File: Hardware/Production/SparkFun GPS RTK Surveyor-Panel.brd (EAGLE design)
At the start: 166 x 248 mm, 778 parts, among them J13 Internal, J16 microSD, J17 Qwiic Right Angle, J19 External, J20 USB Female Type C Connector, J21 Power Switch, J24 Start Base, J25 USB Female Type C Connector, J3 USB Female Type C Connector, J32 microSD, J34 Qwiic Right Angle, J36 Internal, J37 External, J38 USB Female Type C Connector, J39 Power Switch, J4 External, J42 Start Base, J43 USB Female Type C Connector, J5 USB Female Type C Connector, J50 microSD, J52 Qwiic Right Angle, J54 Internal, J55 External, J56 USB Female Type C Connector, J57 Power Switch, J6 Start Base, J60 Start Base, J61 USB Female Type C Connector, J68 microSD, J7 Power Switch, J70 Qwiic Right Angle, J72 Internal, Q1 MBT3904DW1T1, Q2 MBT3904DW1T1, Q3 MBT3904DW1T1, Q4 MBT3904DW1T1, U1 3.3V, U10 MCP73833, U11 CH340C, U12 MAX17048, U13 3.3V, U14 MCP73833, U15 3.3V, U16 U-BLOX_ZED-F9P, U17 ESP-WROOM-32NARROW, U18 CH340C, U19 MAX17048, U2 3.3V, U20 3.3V, U21 MCP73833, U22 3.3V, U23 U-BLOX_ZED-F9P, U24 ESP-WROOM-32NARROW, U25 CH340C, U26 MAX17048, U27 3.3V, U28 MCP73833, U3 U-BLOX_ZED-F9P, U4 3.3V, U5 ESP-WROOM-32NARROW, U6 CH340C, U7 MAX17048, U8 U-BLOX_ZED-F9P, U9 ESP-WROOM-32NARROW

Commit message: 1x3 panel
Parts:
- removed BLUETOOTH_BROADCAST3, SERIAL1_CONNECTION3, ZED_CONTROL3: (no value), SparkFun-Switches:SWITCH_DPDT_SMD_AYZ0202
- removed BT4: LIPO-OUTLINE1100, SparkFun-Batteries:LIPO-1000
- removed C52, C54, C56, C67, C68: 1.0uF, SparkFun-Capacitors:0603
- removed C53, C57, C61, C62, C63, C65, C66: 0.1uF, SparkFun-Capacitors:0603
- removed C55: 47pF, SparkFun-Capacitors:0402
- removed C58, C59: 4.7uF, SparkFun-Capacitors:0603
- removed C60, C64: 10uF, SparkFun-Capacitors:0603
- removed D37: Yellow, SparkFun-LED:LED-0603
- removed D38: WHITE, SparkFun-LED:LED-0603
- removed D39, D48: PRTR5V0U2F, SparkFun-IC-Power:SOT886
- removed D40: RED, SparkFun-LED:LED-0603
- removed D41, D46: 3A/10V/280mV, SparkFun-DiscreteSemi:SOD-323
- removed D42, D43, D44: GREEN, SparkFun-LED:LED-0603
- removed D45: BLUE, SparkFun-LED:LED-0603
- removed D47: RGB, SparkFun-LED:PLCC-6-LED
- removed DUAL_OUTPUT3: (no value), SparkFun-Jumpers:SMT-JUMPER_2_NO_SILK
- removed E4: SMA, SparkFun-RF:SMA-EDGE-SMD
- removed FB4: 2.66Ω, SparkFun-Coils:0402-TIGHT
- removed J55: External, SparkFun-Connectors:JST04_1MM_RA
- removed J56, J61: USB Female Type C Connector, SparkFun-Connectors:USB-C-16P_4LAYER-PADS
- removed J57: Power Switch, SparkFun-Connectors:JST-2-SMD
- removed J58: (no value), SparkFun-Connectors:JST-2-SMD
- removed J59, J67, J69: (no value), SparkFun-Connectors:1X02_NO_SILK
- removed J60: Start Base, SparkFun-Connectors:JST-2-SMD
- removed J62, J63: (no value), SparkFun-Connectors:JST-4-SMD-1.25MM-LOCKING
- removed J64, J65, J66: (no value), SparkFun-Connectors:1X04_NO_SILK
- removed J68: microSD, SparkFun-Connectors:MICRO-SD-SOCKET
- removed J70: Qwiic Right Angle, SparkFun-Connectors:1X04_NO_SILK
- removed J71: (no value), SparkFun-Connectors:1X05_NO_SILK
- removed J72: Internal, SparkFun-Connectors:JST04_1MM_RA
- removed JP10, JP11, JP12, JP9: FIDUCIALUFIDUCIAL, SparkFun-Aesthetics:FIDUCIAL-MICRO
- removed LOGO10: OSHW-LOGOMINI, SparkFun-Aesthetics:OSHW-LOGO-MINI
- removed LOGO11, LOGO12: SFE_LOGO_NAME_FLAME.1_INCH, SparkFun-Aesthetics:SFE_LOGO_NAME_FLAME_.1
- removed MEAS6, MEAS7: (no value), SparkFun-Jumpers:COMBO-JUMPER_2_NC_TRACE
- removed Q4: MBT3904DW1T1, SparkFun-DiscreteSemi:SC70-6
- removed R100, R113, R99: 33, SparkFun-Resistors:1206_RA
- removed R101: 33, SparkFun-Resistors:0603
- removed R102, R112, R94: 330, SparkFun-Resistors:0603
- removed R103, R116, R117: 1k, SparkFun-Resistors:0603
- removed R104, R105, R106, R91: 20, SparkFun-Resistors:0603
- removed R107, R108, R109, R120: 10k, SparkFun-Resistors:0603
- removed R110, R111, R97, R98: 5.1k, SparkFun-Resistors:0603
- removed R114, R96: 100k, SparkFun-Resistors:0603
- removed R115: 4.7k, SparkFun-Resistors:0603
- removed R118: 150k, SparkFun-Resistors:0603
- removed R119: 0, SparkFun-Resistors:0603
- removed R92, R93: 27, SparkFun-Resistors:0603
- removed R95: 10, SparkFun-Resistors:0603
- removed U$277, U$368: (no value), SparkFun-Aesthetics:QWIIC_4MM
- removed U$278: (no value), output:#RTK#0
- removed U$279: (no value), output:#PPS#1
- removed U$280: (no value), output:#PWR#2
- removed U$281, U$309, U$350: (no value), output:#3V3#0
- removed U$282, U$310, U$311, U$353: (no value), output:#GND#0
- removed U$283: (no value), output:ANTENNA0
- removed U$284, U$335: (no value), output:_SURVEYOR3
- removed U$285: (no value), output:#RTK#1
- removed U$286: (no value), output:ACTIVE0
- removed U$287: (no value), output:L1#L21
- removed U$288: (no value), output:#PAIR#0
- removed U$289: (no value), SparkFun GPS RTK Surveyor:1553DBK-ENCLOSURE
- removed U$290: (no value), output:#CHG#0
- removed U$291: (no value), output:LIPO0
- removed U$292: (no value), output:U#BLOX0
- removed U$293, U$348: (no value), output:USB1
- removed U$294: (no value), output:SERIAL20
- removed U$295, U$331: (no value), output:SERIAL10
- removed U$296, U$298: (no value), SparkFun GPS RTK Surveyor:ROCKER_SWITCH
- removed U$297: (no value), output:#BASE#0
- removed U$299, U$300, U$333, U$340, U$341, U$342, U$343, U$344: (no value), SparkFun GPS RTK Surveyor:LIGHT_PIPE_3MM
- removed U$301: (no value), output:BASE2
- removed U$302: (no value), output:OFF1
- removed U$303: (no value), output:ON0
- removed U$304: (no value), output:ROVER3
- removed U$305: (no value), output:#RX2#2
- removed U$306: (no value), output:#TX2#1
- removed U$307, U$352: (no value), output:#RX1#2
- removed U$308, U$351: (no value), output:#TX1#1
- removed U$312, U$325: (no value), output:NMEA1
- removed U$313: (no value), output:RADIO0
- removed U$314: (no value), output:##RST##4
- removed U$315: (no value), output:##SAFE##5
- removed U$316: (no value), output:#FENCE#3
- removed U$317: (no value), output:#INT#0
- removed U$318: (no value), output:BASE0
- removed U$319, U$321: (no value), output:SWITCH1
- removed U$320: (no value), output:POWER0
- removed U$322: (no value), output:#3#5#5V#0
- removed U$323: (no value), output:BLUETOOTH2
- removed U$324: (no value), output:BROADCAST3
- removed U$326: (no value), output:RTCM0
- removed U$327: (no value), output:BLUEOOTH3
- removed U$328: (no value), output:CNTR1
- removed U$329: (no value), output:EXT0
- removed U$330: (no value), output:NMEA2
- removed U$332: (no value), output:CONNECTION1
- removed U$334: (no value), output:#PPS#0
- removed U$336: (no value), output:#RX#2
- removed U$337: (no value), output:ZED0
- removed U$338: (no value), output:#TX#1
- removed U$339: (no value), output:#DUAL#0
- removed U$345: (no value), output:#1CM#0
- removed U$346: (no value), output:#10CM#1
- removed U$347: (no value), output:#100CM#2
- removed U$349: (no value), output:ESP320
- removed U$354: (no value), output:MICROSD0
- removed U$355: (no value), output:#GND#1
- removed U$356: (no value), output:#ESP_RST#0
- removed U$357, U$358: (no value), output:RTK0
- removed U$359: (no value), output:#GND#2
- removed U$360: (no value), output:#3V3#2
- removed U$361: (no value), output:#SCL#1
- removed U$362: (no value), output:#SDA#0
- removed U$363: (no value), output:#D_SEL#0
- removed U$364: (no value), output:DATA2
- removed U$365: (no value), output:PORT3
- removed U$366: (no value), output:PPS#RESET0
- removed U$367: (no value), output:NMEA#SERIAL1
- removed U22, U27: 3.3V, SparkFun-IC-Power:SOT23-5
- removed U23: U-BLOX_ZED-F9P, SparkFun-GPS:ZED-F9P
- removed U24: ESP-WROOM-32NARROW, SparkFun-RF:ESP-WROOM-32-NARROW
- removed U25: CH340C, SparkFun-IC-Comms:SO016
- removed U26: MAX17048, SparkFun-IC-Power:DFN-8
- removed U28: MCP73833, SparkFun-IC-Power:DFN-10
- moved BLUETOOTH_BROADCAST2 180.4 mm to (150.0, 19.0)
- moved BT3 180.4 mm to (197.0, 63.4)
- moved C35 180.4 mm to (174.1, 38.0)
- moved C36 180.4 mm to (171.6, 38.0)
- moved C37 180.4 mm to (180.5, 40.6)
- moved C38 180.4 mm to (167.8, 16.2)
- moved C39 180.4 mm to (176.7, 38.0)
- moved C40 180.4 mm to (172.8, 40.6)
- moved C41 180.4 mm to (153.8, 105.3)
- moved C42 180.4 mm to (153.8, 98.0)
- moved C43 180.4 mm to (156.3, 94.9)
- moved C44 180.4 mm to (181.7, 99.0)
- moved C45 180.4 mm to (184.3, 95.2)
- moved C46 180.4 mm to (183.3, 99.0)
- moved C47 180.4 mm to (156.3, 96.5)
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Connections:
- removed net 3.3V3: C52.1, C53.2, C56.1, C57.2, C60.1, C61.1, C63.1, C64.1, C65.1, J55.2, J63.1, J65.4, J66.4, J68.VCC, J70.2, J72.2, R107.2, R114.2, R94.2, R96.2, U22.5, U23.33, U23.34, U23.38, U24.2, U25.16, U25.4
- removed net 5V3: C54.1, J57.1, J62.1, J64.4, U22.1, U22.3
- removed net ANT_VCC3: C55.1, FB4.2, R95.1
- removed net BACKUP3: C68.1, U23.36, U27.5
- removed net CC13: J56.A5, R98.2
- removed net CC14: J56.B5, R97.2
- removed net CC15: J61.B5, R110.2
- removed net CC16: J61.A5, R111.2
- removed net CHG_LED3: R115.2, U28.3
- removed net CHG_THERM4: R118.2, R119.2, R120.2
- removed net D+6: D39.4, R92.1
- removed net D+7: D48.4, U25.5
- removed net D-6: D39.6, R93.1
- removed net D-7: D48.6, U25.6
- removed net ESP32_!DTR3: Q4.1, R108.1, U25.13
- removed net ESP32_!RTS3: Q4.4, R109.1, U25.14
- removed net ESP32_EN3: C62.1, J69.1, Q4.3, R107.1, U24.3
- removed net ESP32_RXI3: U24.34, U25.2
- removed net ESP32_TXO3: U24.35, U25.3
- removed net ESP_0/BOOT3: Q4.6, U24.25
- removed net ESP_12/LED_BLUETOOTH3: R112.1, U24.14
- removed net ESP_13/LED_100CM3: R104.1, U24.16
- removed net ESP_15/LED_10CM3: R105.1, U24.23
- removed net ESP_16/BT_RXI3: BLUETOOTH_BROADCAST3.2, U24.27
- removed net ESP_17/BT_TXO3: BLUETOOTH_BROADCAST3.5, U24.28
- removed net ESP_18/SD_SCK3: J68.SCLK, U24.30
- removed net ESP_19/SD_CIPO3: J68.DO/DAT0, U24.31
- removed net ESP_2/LED_1CM3: R106.1, U24.24
- removed net ESP_21/SDA3: J55.3, J70.3, J72.3, R99.P6, U24.33, U26.8
- removed net ESP_22/SCL3: J55.4, J70.4, J72.4, R99.P7, U24.36, U26.7
- removed net ESP_23/SD_COPI3: J68.DI/CMD, U24.37
- removed net ESP_25/SD_!CS!3: J68.CS/DAT3, R114.1, U24.10
- removed net ESP_26/ZED_TX_READY3: J71.1, R99.P8, U24.11
- removed net ESP_26/ZED_TX_READY_LV3: R99.P1, U23.46
- removed net ESP_27/ZED_!RESET!3: J71.2, R100.P5, U24.12, ZED_CONTROL3.4
- removed net ESP_27/ZED_!RESET!_LV3: R100.P4, U23.49
- removed net ESP_3: U24.13
- removed net ESP_32/PWR_LVL_RED3: D47.AR, U24.8
- removed net ESP_33/PWR_LVL_GRN3: D47.AG, U24.9
- removed net ESP_36/BATT_ALRT3: U24.4, U26.5
- removed net ESP_4/LED_BASE_STAT3: R102.1, U24.26
- removed net ESP_5/SWITCH_BASE_SELECT3: J60.1, U24.29
- removed net ESP_D1+3: D48.3, J61.A6, J61.B6
- removed net ESP_D1-3: D48.1, J61.A7, J61.B7
- removed net ESP_I7: U24.5
- removed net ESP_I8: U24.6
- removed net ESP_I9: U24.7
- removed net EXTERNAL_SERIAL1_RXI/ZED_!RESET!3: J63.3, J65.2, ZED_CONTROL3.5
- removed net EXTERNAL_SERIAL1_RXI3: SERIAL1_CONNECTION3.4, ZED_CONTROL3.6
- removed net EXTERNAL_SERIAL1_TXO/PPS3: J63.2, J65.3, ZED_CONTROL3.2
- removed net EXTERNAL_SERIAL1_TXO3: DUAL_OUTPUT3.2, SERIAL1_CONNECTION3.1, ZED_CONTROL3.3
- removed net FENCE_LV3: R113.P8, U23.19
- removed net GND3: C52.2, C53.1, C54.2, C55.2, C56.2, C57.1, C58.2, C59.2, C60.2, C61.2, C62.2, C63.2, C64.2, C65.2, C66.2, C67.2, C68.2, D37.C, D39.2, D40.C, D42.C, D43.C, D44.C, D45.C, D48.2, E4.GND@0, E4.GND@1, J55.1, J56.GND, J56.GND2, J56.SHLD1, J56.SHLD2, J56.SHLD3, J56.SHLD4, J58.1, J59.2, J60.2, J61.GND, J61.GND2, J61.SHLD1, J61.SHLD2, J61.SHLD3, J61.SHLD4, J62.4, J63.4, J64.1, J65.1, J66.1, J68.CD1, J68.GND, J68.GND1, J68.GND3, J69.2, J70.1, J72.1, R103.1, R110.1, R111.1, R116.2, R117.2, R118.1, R120.1, R96.1, R97.1, R98.1, U22.2, U23.1, U23.100, U23.101, U23.102, U23.12, U23.14, U23.3, U23.32, U23.37, U23.41, U23.48, U23.55, U23.56, U23.57, U23.58, U23.59, U23.60, U23.61, U23.62, U23.63, U23.64, U23.65, U23.66, U23.67, U23.68, U23.69, U23.70, U23.71, U23.72, U23.73, U23.74, U23.75, U23.76, U23.77, U23.78, U23.79, U23.80, U23.81, U23.82, U23.83, U23.84, U23.85, U23.86, U23.87, U23.88, U23.89, U23.90, U23.91, U23.92, U23.93, U23.94, U23.95, U23.96, U23.97, U23.98, U23.99, U24.1, U24.15, U24.38, U24.GND, U25.1, U26.1, U26.4, U26.6, U26.9, U27.2, U28.11, U28.5
- removed net GPS_ANT4: E4.SIG, FB4.1, U23.2
- removed net LIPO_RAW3: J58.2, MEAS7.1, MEAS7.3
- removed net N$55: D37.A, R91.1
- removed net N$56: R92.2, U23.40
- removed net N$57: R93.2, U23.39
- removed net N$58: D38.A, R94.1
- removed net N$59: R95.2, U23.7
- removed net N$60: D40.A, R102.2
- removed net N$61: D42.A, R104.2
- removed net N$62: D43.A, R105.2
- removed net N$63: D44.A, R106.2
- removed net N$64: Q4.5, R108.2
- removed net N$65: Q4.2, R109.2
- removed net N$66: D46.A, J61.VBUS1, J61.VBUS2
- removed net N$67: D45.A, R112.2
- removed net N$68: J56.VBUS1, J56.VBUS2, MEAS6.1, MEAS6.3
- removed net N$69: D47.CG, R116.1
- removed net N$70: D47.CR, R117.1
- removed net N$71: D47.CB, R115.1
- removed net N$72: R119.1, U28.8
- removed net NMEA-RX3: BLUETOOTH_BROADCAST3.6, SERIAL1_CONNECTION3.6
- removed net NMEA-TX3: BLUETOOTH_BROADCAST3.3, DUAL_OUTPUT3.1, SERIAL1_CONNECTION3.3
- removed net PPS3: R100.P1, U23.53
- removed net PROG4: R103.2, U28.6
- removed net RTK_LV3: R113.P7, U23.20
- removed net RX2_LV3: R113.P6, U23.26
- removed net RXLV3: R99.P4, U23.43
- removed net SCL_LV3: R99.P2, U23.45
- removed net SDA_LV3: R99.P3, U23.44
- removed net TX2_LV3: R113.P5, U23.27
- removed net TXLV3: R101.1, U23.42
- removed net UNP_D+3: D39.3, J56.A6, J56.B6
- removed net UNP_D-3: D39.1, J56.A7, J56.B7
- removed net VIN3: C59.1, D39.5, D41.C, D46.C, D47.AB, D48.5, J57.2, MEAS6.2, MEAS6.4, U28.1, U28.2
- removed net V_BATT3: C58.1, C66.1, C67.1, D41.A, J59.1, MEAS7.2, MEAS7.4, U26.2, U26.3, U27.1, U27.3, U28.10, U28.9
- removed net ZED-RXI7: BLUETOOTH_BROADCAST3.4, J62.3, J64.2, R113.P3
- removed net ZED-RXI8: J67.2, R99.P5, SERIAL1_CONNECTION3.5
- removed net ZED-TXO7: J67.1, R101.2, SERIAL1_CONNECTION3.2
- removed net ZED-TXO8: BLUETOOTH_BROADCAST3.1, J62.2, J64.3, R113.P4
- removed net ZED_!SAFE!3: J71.3, R100.P6
- removed net ZED_!SAFE!_LV3: R100.P3, U23.50
- removed net ZED_D_SEL3: J71.5, R100.P7
- removed net ZED_D_SEL_LV3: R100.P2, U23.47
- removed net ZED_FENCE_STAT3: J66.2, R113.P1
- removed net ZED_PPS_STAT3: J71.4, R100.P8, R91.2, ZED_CONTROL3.1
- removed net ZED_RTK_STAT3: D38.C, J66.3, R113.P2
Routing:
- net 3.3V3: track 297.3 -> 0.00 mm, vias 8 -> 0
- net ESP_22/SCL3: track 203.8 -> 0.00 mm, vias 8 -> 0
- net ESP_21/SDA3: track 199.8 -> 0.00 mm, vias 8 -> 0
- net VIN3: track 189.6 -> 0.00 mm, vias 9 -> 0
- net ESP_23/SD_COPI3: track 120.9 -> 0.00 mm, vias 3 -> 0
- net ESP_19/SD_CIPO3: track 115.8 -> 0.00 mm, vias 3 -> 0
- net ESP_18/SD_SCK3: track 113.2 -> 0.00 mm, vias 3 -> 0
- net 5V3: track 112.3 -> 0.00 mm, vias 2 -> 0
- net ESP_25/SD_!CS!3: track 109.8 -> 0.00 mm, vias 3 -> 0
- net D+7: track 103.1 -> 0.00 mm, vias 3 -> 0
- net ESP_27/ZED_!RESET!3: track 102.6 -> 0.00 mm, vias 4 -> 0
- net EXTERNAL_SERIAL1_TXO/PPS3: track 101.6 -> 0.00 mm, vias 2 -> 0
- net D-7: track 100.9 -> 0.00 mm, vias 3 -> 0
- net CHG_LED3: track 100.1 -> 0.00 mm, vias 4 -> 0
- net EXTERNAL_SERIAL1_RXI/ZED_!RESET!3: track 99.7 -> 0.00 mm, vias 3 -> 0
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- removed copper zone on layer 1, net GND3
- removed copper zone on layer 15, net GND3
- removed copper zone on layer 16, net GND3
- removed copper zone on layer 2, net GND3
- removed copper zone on layer 16, net VIN3
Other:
- board size 166 x 248 mm -> 226.8 x 137.8 mm
- board text added: "v-score"

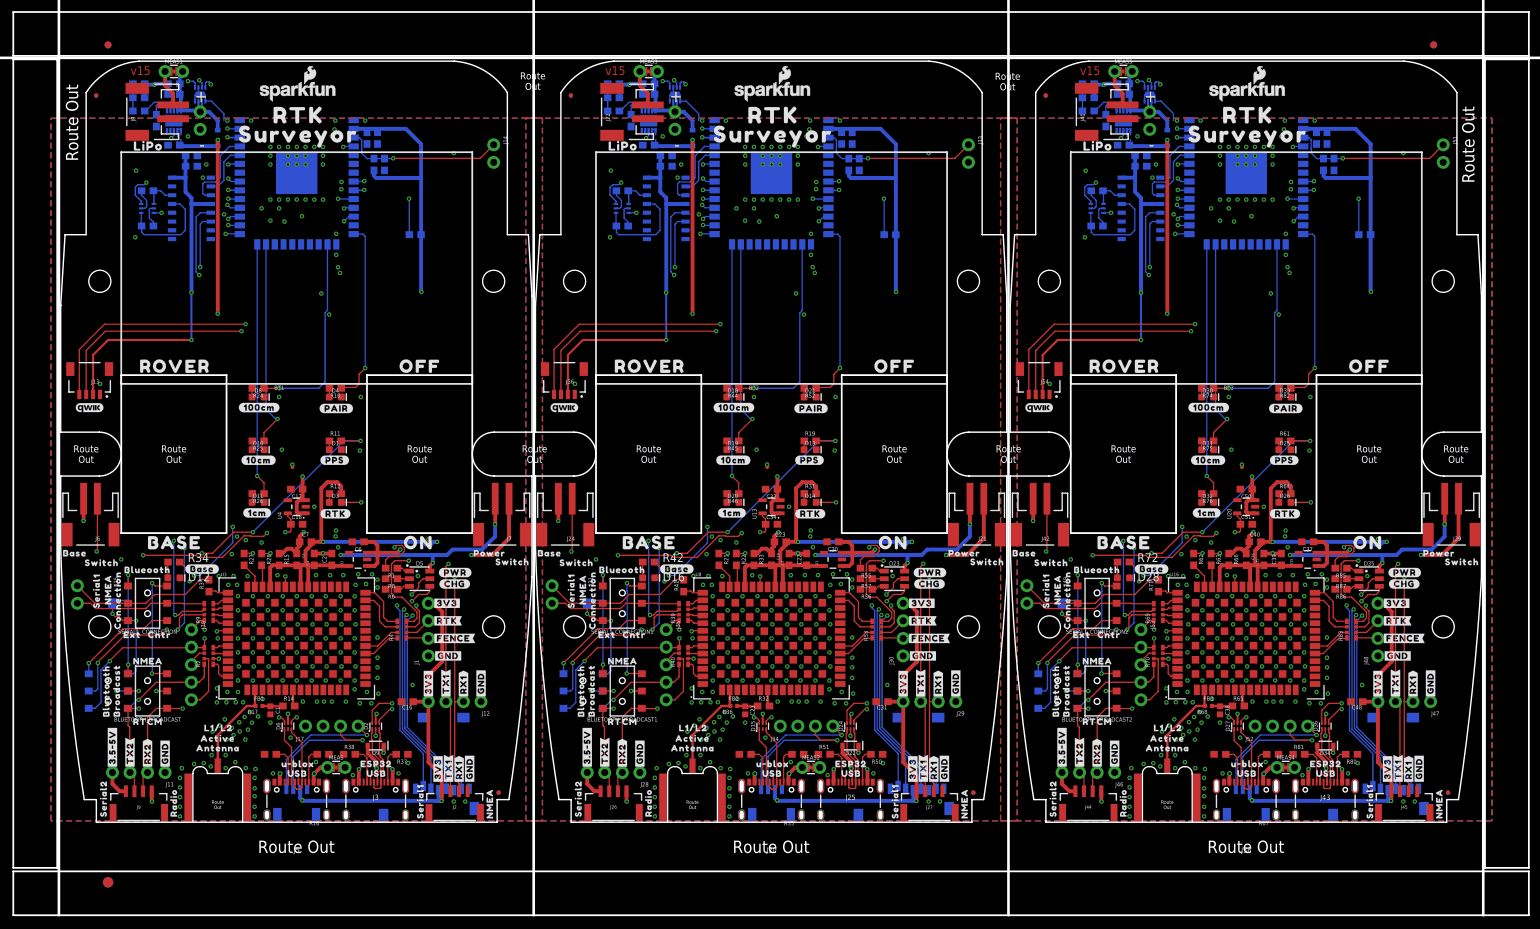
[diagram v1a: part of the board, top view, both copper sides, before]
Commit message: Move fiducials on production panel
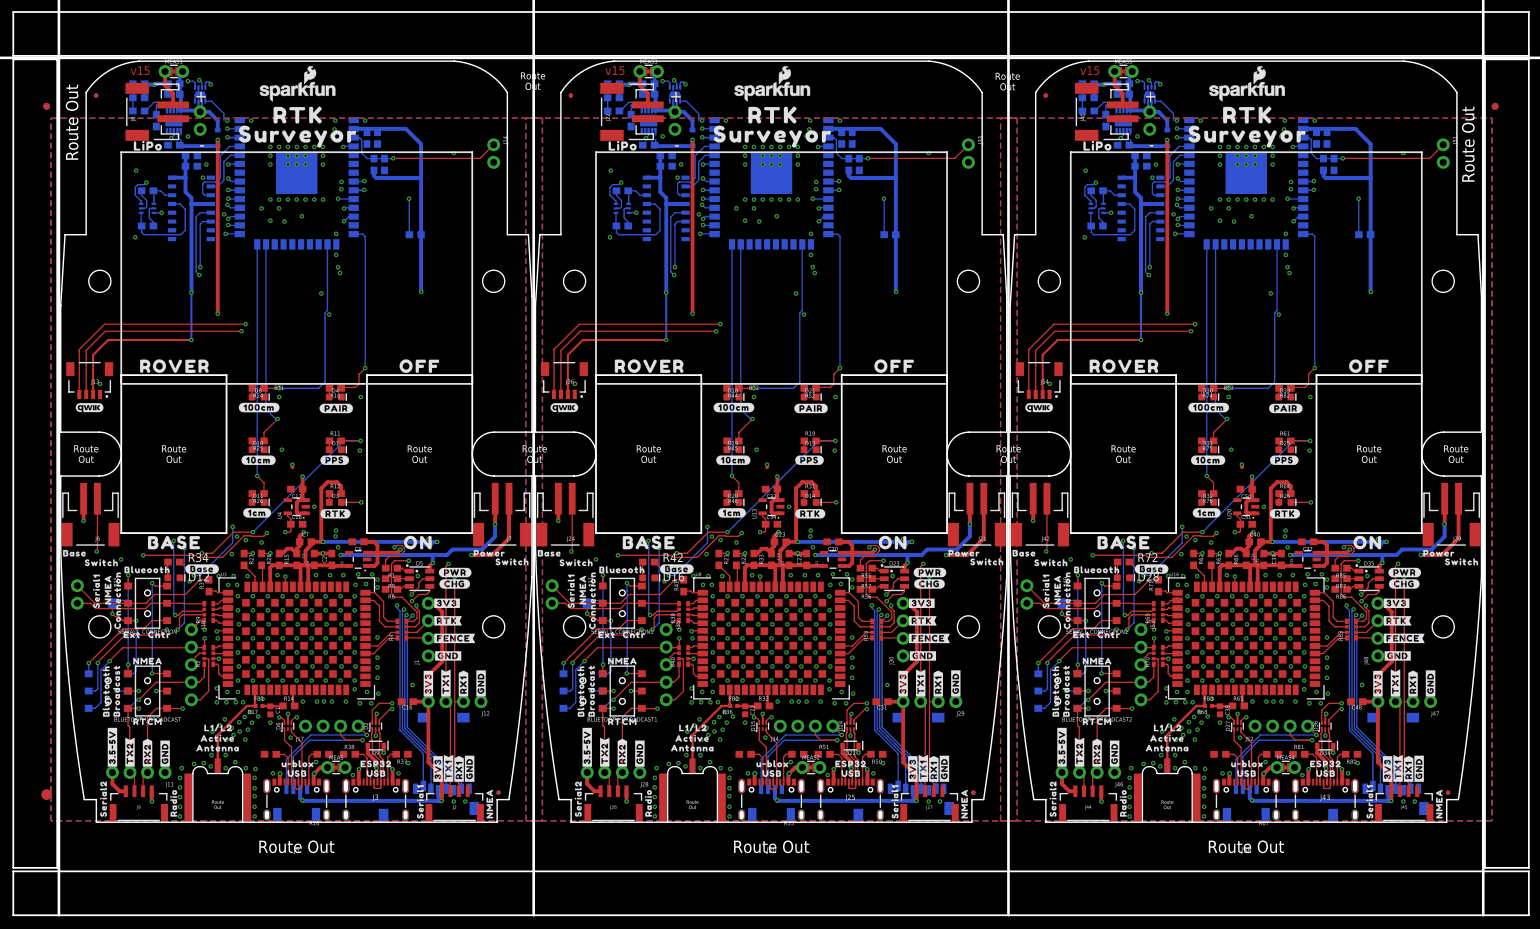
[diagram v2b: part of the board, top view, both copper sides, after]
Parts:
- moved E$5 15.5 mm to (-2.03, 4.00)
- moved E$6 15.5 mm to (-2.03, 4.00)
- moved E$3 12.6 mm to (207.6, 103.6)
- moved E$4 12.6 mm to (207.6, 103.6)
- moved E$1 12.6 mm to (-2.03, 103.6)
- moved E$2 12.6 mm to (-2.03, 103.6)
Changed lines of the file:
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@@
 <layers>
 <layer number="1" name="Top" color="4" fill="1" visible="yes" active="yes"/>
-<layer number="2" name="Route2" color="16" fill="1" visible="yes" active="yes"/>
+<layer number="2" name="Route2" color="16" fill="1" visible="no" active="yes"/>
 <layer number="3" name="Route3" color="17" fill="1" visible="no" active="no"/>
 <layer number="4" name="Route4" color="18" fill="1" visible="no" active="no"/>
@@
 <layer number="13" name="Route13" color="21" fill="1" visible="no" active="no"/>
 <layer number="14" name="Route14" color="22" fill="1" visible="no" active="no"/>
-<layer number="15" name="Route15" color="23" fill="1" visible="yes" active="yes"/>
+<layer number="15" name="Route15" color="23" fill="1" visible="no" active="yes"/>
 <layer number="16" name="Bottom" color="1" fill="1" visible="yes" active="yes"/>
 <layer number="17" name="Pads" color="2" fill="1" visible="yes" active="yes"/>
@@
 <layer number="19" name="Unrouted" color="6" fill="1" visible="yes" active="yes"/>
 <layer number="20" name="Dimension" color="24" fill="1" visible="yes" active="yes"/>
-<layer number="21" name="tPlace" color="7" fill="1" visible="yes" active="yes"/>
-<layer number="22" name="bPlace" color="7" fill="1" visible="yes" active="yes"/>
+<layer number="21" name="tPlace" color="16" fill="1" visible="yes" active="yes"/>
+<layer number="22" name="bPlace" color="14" fill="1" visible="yes" active="yes"/>
 <layer number="23" name="tOrigins" color="15" fill="1" visible="yes" active="yes"/>
 <layer number="24" name="bOrigins" color="15" fill="1" visible="yes" active="yes"/>
-<layer number="25" name="tNames" color="7" fill="1" visible="yes" active="yes"/>
-<layer number="26" name="bNames" color="7" fill="1" visible="yes" active="yes"/>
-<layer number="27" name="tValues" color="7" fill="1" visible="yes" active="yes"/>
-<layer number="28" name="bValues" color="7" fill="1" visible="yes" active="yes"/>
-<layer number="29" name="tStop" color="7" fill="3" visible="yes" active="yes"/>
-<layer number="30" name="bStop" color="7" fill="6" visible="yes" active="yes"/>
-<layer number="31" name="tCream" color="7" fill="4" visible="yes" active="yes"/>
-<layer number="32" name="bCream" color="7" fill="5" visible="yes" active="yes"/>
-<layer number="33" name="tFinish" color="6" fill="3" visible="yes" active="yes"/>
-<layer number="34" name="bFinish" color="6" fill="6" visible="yes" active="yes"/>
-<layer number="35" name="tGlue" color="7" fill="4" visible="yes" active="yes"/>
-<layer number="36" name="bGlue" color="7" fill="5" visible="yes" active="yes"/>
-<layer number="37" name="tTest" color="7" fill="1" visible="yes" active="yes"/>
-<layer number="38" name="bTest" color="7" fill="1" visible="yes" active="yes"/>
-<layer number="39" name="tKeepout" color="4" fill="11" visible="yes" active="yes"/>
-<layer number="40" name="bKeepout" color="1" fill="11" visible="yes" active="yes"/>
-<layer number="41" name="tRestrict" color="4" fill="10" visible="yes" active="yes"/>
-<layer number="42" name="bRestrict" color="1" fill="10" visible="yes" active="yes"/>
-<layer number="43" name="vRestrict" color="2" fill="10" visible="yes" active="yes"/>
-<layer number="44" name="Drills" color="7" fill="1" visible="yes" active="yes"/>
+<layer number="25" name="tNames" color="7" fill="1" visible="no" active="yes"/>
+<layer number="26" name="bNames" color="7" fill="1" visible="no" active="yes"/>
+<layer number="27" name="tValues" color="7" fill="1" visible="no" active="yes"/>
+<layer number="28" name="bValues" color="7" fill="1" visible="no" active="yes"/>
+<layer number="29" name="tStop" color="7" fill="3" visible="no" active="yes"/>
+<layer number="30" name="bStop" color="7" fill="6" visible="no" active="yes"/>
+<layer number="31" name="tCream" color="7" fill="4" visible="no" active="yes"/>
+<layer number="32" name="bCream" color="7" fill="5" visible="no" active="yes"/>
+<layer number="33" name="tFinish" color="6" fill="3" visible="no" active="yes"/>
+<layer number="34" name="bFinish" color="6" fill="6" visible="no" active="yes"/>
+<layer number="35" name="tGlue" color="7" fill="4" visible="no" active="yes"/>
+<layer number="36" name="bGlue" color="7" fill="5" visible="no" active="yes"/>
+<layer number="37" name="tTest" color="7" fill="1" visible="no" active="yes"/>
+<layer number="38" name="bTest" color="7" fill="1" visible="no" active="yes"/>
+<layer number="39" name="tKeepout" color="4" fill="11" visible="no" active="yes"/>
+<layer number="40" name="bKeepout" color="1" fill="11" visible="no" active="yes"/>
+<layer number="41" name="tRestrict" color="4" fill="10" visible="no" active="yes"/>
+<layer number="42" name="bRestrict" color="1" fill="10" visible="no" active="yes"/>
+<layer number="43" name="vRestrict" color="2" fill="10" visible="no" active="yes"/>
+<layer number="44" name="Drills" color="7" fill="1" visible="no" active="yes"/>
 <layer number="45" name="Holes" color="7" fill="1" visible="yes" active="yes"/>
-<layer number="46" name="Milling" color="3" fill="1" visible="yes" active="yes"/>
-<layer number="47" name="Measures" color="7" fill="1" visible="yes" active="yes"/>
-<layer number="48" name="Document" color="7" fill="1" visible="yes" active="yes"/>
-<layer number="49" name="Reference" color="7" fill="1" visible="yes" active="yes"/>
-<layer number="50" name="dxf" color="7" fill="1" visible="yes" active="yes"/>
-<layer number="51" name="tDocu" color="7" fill="1" visible="yes" active="yes"/>
-<layer number="52" name="bDocu" color="7" fill="1" visible="yes" active="yes"/>
+<layer number="46" name="Milling" color="3" fill="1" visible="no" active="yes"/>
+<layer number="47" name="Measures" color="7" fill="1" visible="no" active="yes"/>
+<layer number="48" name="Document" color="7" fill="1" visible="no" active="yes"/>
+<layer number="49" name="Reference" color="7" fill="1" visible="no" active="yes"/>
+<layer number="50" name="dxf" color="7" fill="1" visible="no" active="yes"/>
+<layer number="51" name="tDocu" color="6" fill="1" visible="yes" active="yes"/>
+<layer number="52" name="bDocu" color="7" fill="1" visible="no" active="yes"/>
 <layer number="53" name="tGND_GNDA" color="7" fill="9" visible="no" active="no"/>
 <layer number="54" name="bGND_GNDA" color="1" fill="9" visible="no" active="no"/>
@@
 </element>
 <element name="U$276" library="SparkFun-Aesthetics" package="QWIIC_4MM" value="" x="141.605" y="59.988959375" smashed="yes"/>
-<element name="E$1" library="SparkFun-Aesthetics" package="FIDUCIAL-1X2" value="" x="6.858" y="112.48898125" smashed="yes"/>
-<element name="E$2" library="SparkFun-Aesthetics" package="FIDUCIAL-1X2" value="" x="6.858" y="112.48898125" smashed="yes" rot="MR0"/>
-<element name="E$3" library="SparkFun-Aesthetics" package="FIDUCIAL-1X2" value="" x="198.6915" y="112.48898125" smashed="yes"/>
-<element name="E$4" library="SparkFun-Aesthetics" package="FIDUCIAL-1X2" value="" x="198.6915" y="112.48898125" smashed="yes" rot="MR0"/>
-<element name="E$5" library="SparkFun-Retired" package="FIDUCIAL-1.5X3" value="" x="6.858" y="-8.6995" smashed="yes"/>
-<element name="E$6" library="SparkFun-Retired" package="FIDUCIAL-1.5X3" value="" x="6.858" y="-8.6995" smashed="yes" rot="MR0"/>
+<element name="E$1" library="SparkFun-Aesthetics" package="FIDUCIAL-1X2" value="" x="-2.032" y="103.59898125" smashed="yes"/>
+<element name="E$2" library="SparkFun-Aesthetics" package="FIDUCIAL-1X2" value="" x="-2.032" y="103.59898125" smashed="yes" rot="MR0"/>
+<element name="E$3" library="SparkFun-Aesthetics" package="FIDUCIAL-1X2" value="" x="207.5815" y="103.59898125" smashed="yes"/>
+<element name="E$4" library="SparkFun-Aesthetics" package="FIDUCIAL-1X2" value="" x="207.5815" y="103.59898125" smashed="yes" rot="MR0"/>
+<element name="E$5" library="SparkFun-Retired" package="FIDUCIAL-1.5X3" value="" x="-2.032" y="4.0005" smashed="yes"/>
+<element name="E$6" library="SparkFun-Retired" package="FIDUCIAL-1.5X3" value="" x="-2.032" y="4.0005" smashed="yes" rot="MR0"/>
 </elements>
 <signals>
